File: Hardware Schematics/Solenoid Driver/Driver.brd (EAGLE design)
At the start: 21.6 x 21.6 mm, 6 parts

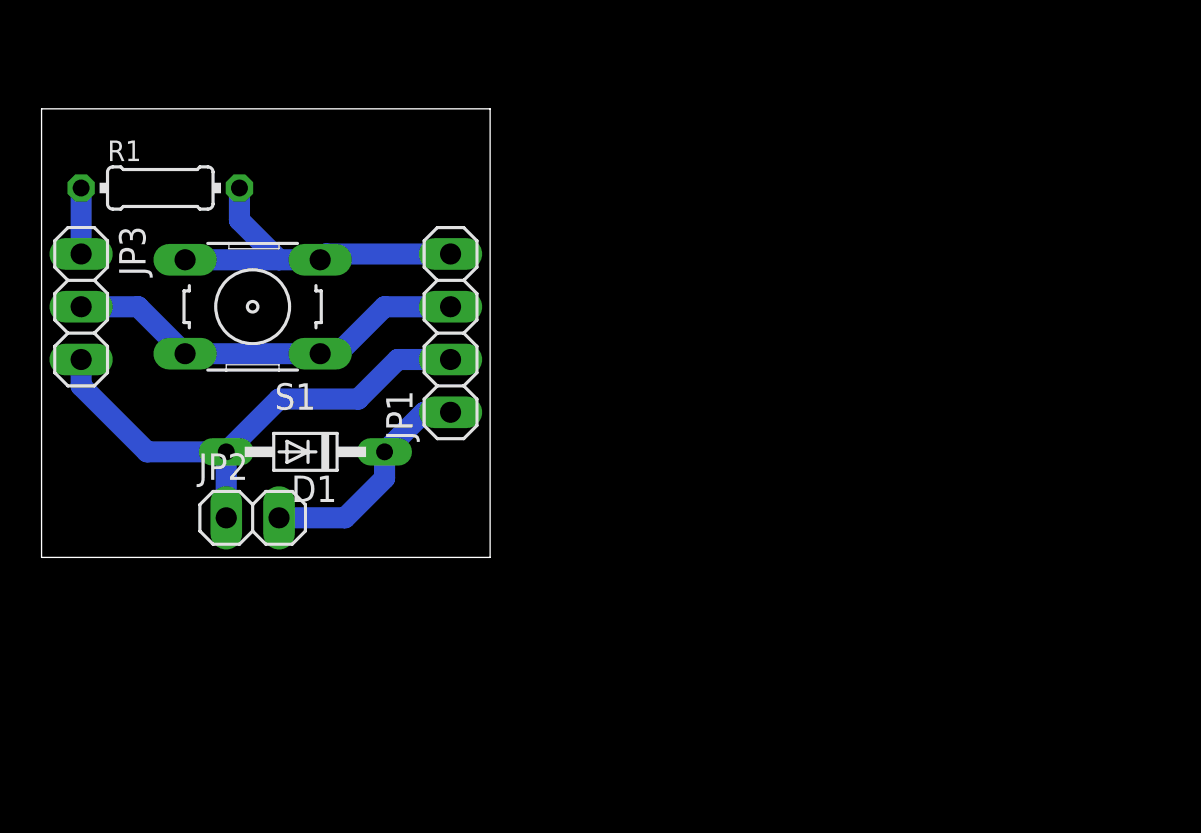
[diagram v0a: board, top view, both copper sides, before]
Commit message: New Solenoid Driver Design
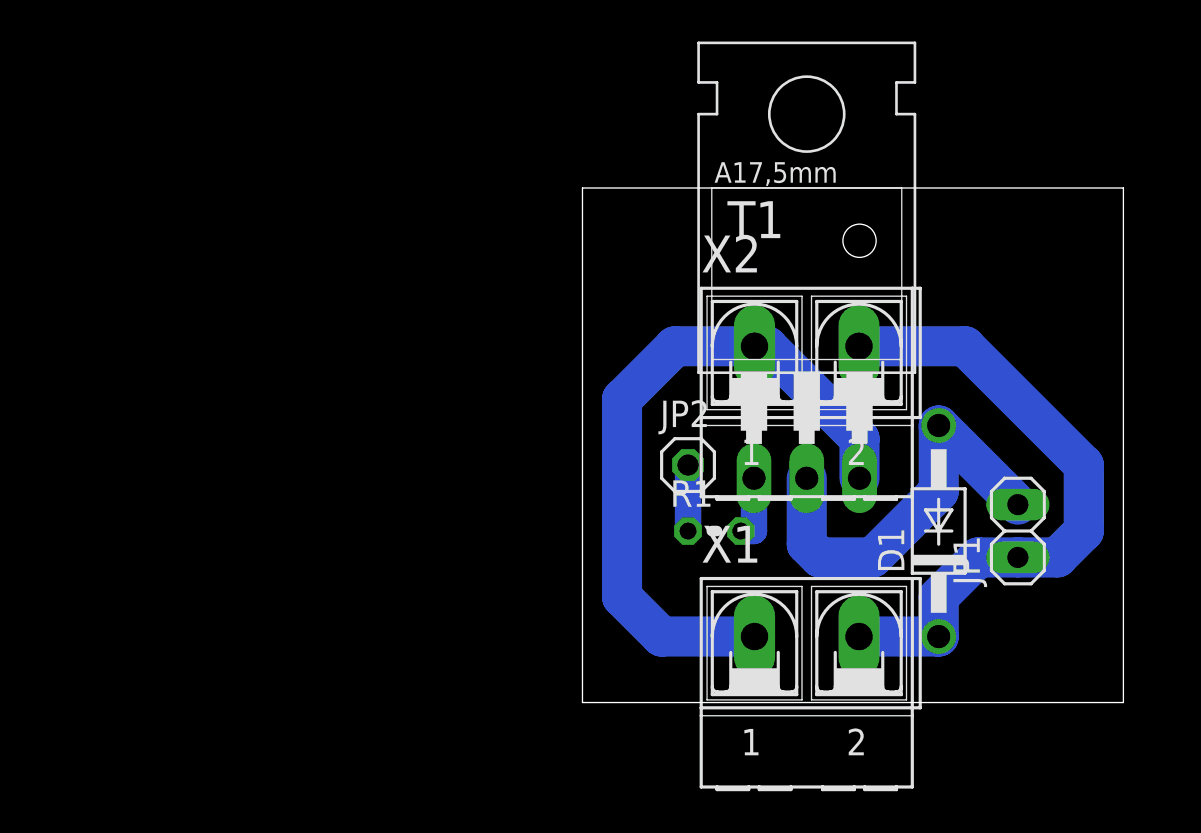
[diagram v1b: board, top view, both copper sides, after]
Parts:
- removed JP3: (no value), pinhead:1X03
- removed S1: (no value), switch-omron:B3F-10XX
- added T1: TIP31, transistor:TO220
- added X1, X2: (no value), con-ptr500:AK500/2-H
- D1: value BAT81 -> 1N4004; device diode:DO34-7 -> diode:DO41-10
- JP1: device pinhead:1X04 -> pinhead:1X02
- JP2: device pinhead:1X02 -> pinhead:1X01
- R1: device resistor:0204/7 -> rcl:0204V
- moved R1 31.4 mm to (46.4, 38.1)
- moved D1 30.7 mm to (57.1, 38.1), turned to 90 degrees
- moved JP1 28.9 mm to (61.0, 38.1)
- moved JP2 21.1 mm to (45.1, 41.3)
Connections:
- removed net ANALOG: JP1.4, R1.2, S1.3, S1.4
- removed net GND: JP1.3, JP3.2, S1.1, S1.2
- removed net L+: D1.C, JP1.1, JP2.2
- removed net L-: D1.A, JP1.2, JP2.1, JP3.3
- new net N$1: D1.A, JP1.2, T1.2
- new net N$3: T1.3, X1.1, X2.1
- new net N$4: JP2.1, R1.1
- new net N$5: D1.C, JP1.1, X1.2, X2.2
- net N$2: now also R1.2, T1.1; no longer JP3.1, R1.1
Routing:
- net N$3: track 0.00 -> 32.9 mm
- net N$5: track 0.00 -> 30.4 mm
- net L-: track 25.4 -> 0.00 mm
- net N$1: track 0.00 -> 19.7 mm
- net GND: track 19.7 -> 0.00 mm
- net ANALOG: track 17.1 -> 0.00 mm
- net L+: track 11.1 -> 0.00 mm
- net N$4: track 0.00 -> 3.17 mm
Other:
- board size 21.6 x 21.6 mm -> 26 x 24.8 mm

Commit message: Updating Repository
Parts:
- removed JP1: (no value), pinhead:1X02
- added X3: (no value), con-ptr500:AK500/2-H
- moved JP2 6.38 mm to (44.5, 34.9)
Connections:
- net N$3 renamed GND
- net N$1: now also X3.2; no longer JP1.2
- net N$5: now also X3.1; no longer JP1.1
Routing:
- net GND: track 32.9 -> 0.00 mm
- net N$1: track 19.7 -> 17.5 mm
- net N$5: track 30.4 -> 29.7 mm
- added copper zone on layer 16, net GND
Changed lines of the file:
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@@
 <layer number="16" name="Bottom" color="1" fill="1" visible="yes" active="yes"/>
 <layer number="17" name="Pads" color="2" fill="1" visible="yes" active="yes"/>
-<layer number="18" name="Vias" color="2" fill="1" visible="no" active="yes"/>
+<layer number="18" name="Vias" color="2" fill="1" visible="yes" active="yes"/>
 <layer number="19" name="Unrouted" color="6" fill="1" visible="no" active="yes"/>
 <layer number="20" name="Dimension" color="15" fill="1" visible="yes" active="yes"/>
@@
 </class>
 </classes>
-<designrules name="default">
+<designrules name="default *">
 <description language="de">&lt;b&gt;EAGLE Design Rules&lt;/b&gt;
 &lt;p&gt;
@@
 <param name="mtCopper" value="0.035mm 0.035mm 0.035mm 0.035mm 0.035mm 0.035mm 0.035mm 0.035mm 0.035mm 0.035mm 0.035mm 0.035mm 0.035mm 0.035mm 0.035mm 0.035mm"/>
 <param name="mtIsolate" value="1.5mm 0.15mm 0.2mm 0.15mm 0.2mm 0.15mm 0.2mm 0.15mm 0.2mm 0.15mm 0.2mm 0.15mm 0.2mm 0.15mm 0.2mm"/>
-<param name="mdWireWire" value="8mil"/>
-<param name="mdWirePad" value="8mil"/>
+<param name="mdWireWire" value="24mil"/>
+<param name="mdWirePad" value="24mil"/>
 <param name="mdWireVia" value="8mil"/>
 <param name="mdPadPad" value="8mil"/>
@@
 <param name="mdViaViaSameLayer" value="8mil"/>
 <param name="mnLayersViaInSmd" value="2"/>
-<param name="mdCopperDimension" value="40mil"/>
-<param name="mdDrill" value="8mil"/>
+<param name="mdCopperDimension" value="24mil"/>
+<param name="mdDrill" value="24mil"/>
 <param name="mdSmdStop" value="0mil"/>
-<param name="msWidth" value="10mil"/>
+<param name="msWidth" value="24mil"/>
 <param name="msDrill" value="24mil"/>
 <param name="msMicroVia" value="9.99mm"/>
@@
 <param name="srMinRoundness" value="0mil"/>
 <param name="srMaxRoundness" value="0mil"/>
-<param name="slThermalIsolate" value="10mil"/>
+<param name="slThermalIsolate" value="0mil"/>
 <param name="slThermalsForVias" value="0"/>
 <param name="dpMaxLengthDifference" value="10mm"/>
@@
 <elements>
 <element name="D1" library="diode" package="DO41-10" value="1N4004" x="57.15" y="38.1" rot="R90"/>
-<element name="JP1" library="pinhead" package="1X02" value="" x="60.96" y="38.1" rot="R90"/>
-<element name="JP2" library="pinhead" package="1X01" value="" x="45.085" y="41.275"/>
+<element name="JP2" library="pinhead" package="1X01" value="" x="44.45" y="34.925"/>
 <element name="R1" library="rcl" package="0204V" value="" x="46.355" y="38.1"/>
 <element name="T1" library="transistor" package="TO220" value="TIP31" x="50.8" y="46.99"/>
@@
 <attribute name="MPN" value="" x="50.8" y="46.99" size="1.778" layer="27" display="off"/>
 </element>
+<element name="X3" library="con-ptr500" package="AK500/2-H" value="" x="60.325" y="37.465" rot="R90">
+<attribute name="OC_NEWARK" value="unknown" x="60.325" y="37.465" size="1.778" layer="27" rot="R90" display="off"/>
+<attribute name="MPN" value="" x="60.325" y="37.465" size="1.778" layer="27" rot="R90" display="off"/>
+<attribute name="OC_FARNELL" value="unknown" x="60.325" y="37.465" size="1.778" layer="27" rot="R90" display="off"/>
+<attribute name="MF" value="" x="60.325" y="37.465" size="1.778" layer="27" rot="R90" display="off"/>
+</element>
 </elements>
 <signals>
@@
 <contactref element="D1" pad="A"/>
 <contactref element="T1" pad="2"/>
-<contactref element="JP1" pad="2"/>
-<wire x1="60.96" y1="39.37" x2="57.15" y2="43.18" width="1.9304" layer="16"/>
 <wire x1="57.15" y1="43.18" x2="57.15" y2="40.005" width="1.9304" layer="16"/>
 <wire x1="57.15" y1="40.005" x2="53.975" y2="36.83" width="1.9304" layer="16"/>
@@
 <wire x1="51.435" y1="36.83" x2="50.8" y2="37.465" width="1.9304" layer="16"/>
 <wire x1="50.8" y1="37.465" x2="50.8" y2="40.64" width="1.9304" layer="16"/>
+<contactref element="X3" pad="2"/>
+<wire x1="60.325" y1="39.9796" x2="57.15" y2="39.9796" width="1.9304" layer="16"/>
+<wire x1="57.15" y1="39.9796" x2="57.15" y2="40.005" width="1.9304" layer="16"/>
 </signal>
 <signal name="N$2">
@@
 <signal name="N$5">
 <contactref element="D1" pad="C"/>
-<contactref element="JP1" pad="1"/>
 <contactref element="X1" pad="2"/>
 <contactref element="X2" pad="2"/>
-<wire x1="57.15" y1="33.02" x2="57.15" y2="34.925" width="1.9304" layer="16"/>
-<wire x1="57.15" y1="34.925" x2="59.055" y2="36.83" width="1.9304" layer="16"/>
-<wire x1="59.055" y1="36.83" x2="60.96" y2="36.83" width="1.9304" layer="16"/>
 <wire x1="53.3146" y1="33.02" x2="57.15" y2="33.02" width="1.9304" layer="16"/>
-<wire x1="60.96" y1="36.83" x2="62.865" y2="36.83" width="1.9304" layer="16"/>
-<wire x1="62.865" y1="36.83" x2="64.135" y2="38.1" width="1.9304" layer="16"/>
-<wire x1="64.135" y1="38.1" x2="64.135" y2="41.275" width="1.9304" layer="16"/>
+<wire x1="64.135" y1="37.465" x2="64.135" y2="41.275" width="1.9304" layer="16"/>
 <wire x1="64.135" y1="41.275" x2="58.42" y2="46.99" width="1.9304" layer="16"/>
 <wire x1="58.42" y1="46.99" x2="53.3146" y2="46.99" width="1.9304" layer="16"/>
+<contactref element="X3" pad="1"/>
+<wire x1="64.135" y1="37.465" x2="61.595" y2="34.925" width="1.9304" layer="16"/>
+<wire x1="61.595" y1="34.925" x2="60.3504" y2="34.925" width="1.9304" layer="16"/>
+<wire x1="60.3504" y1="34.925" x2="60.325" y2="34.9504" width="1.9304" layer="16"/>
+<wire x1="57.15" y1="33.02" x2="58.3946" y2="33.02" width="1.9304" layer="16"/>
+<wire x1="58.3946" y1="33.02" x2="60.325" y2="34.9504" width="1.9304" layer="16"/>
 </signal>
 <signal name="N$4">
 <contactref element="R1" pad="1"/>
 <contactref element="JP2" pad="1"/>
-<wire x1="45.085" y1="38.1" x2="45.085" y2="41.275" width="1.27" layer="16"/>
-</signal>
-<signal name="N$3">
+<wire x1="45.085" y1="38.1" x2="44.45" y2="37.465" width="1.27" layer="16"/>
+<wire x1="44.45" y1="37.465" x2="44.45" y2="34.925" width="1.27" layer="16"/>
+</signal>
+<signal name="GND">
+<polygon width="0.4064" layer="16" orphans="yes">
+<vertex x="40.005" y="54.61"/>
+<vertex x="66.04" y="54.61"/>
+<vertex x="66.04" y="29.845"/>
+<vertex x="40.005" y="29.845"/>
+</polygon>
 <contactref element="T1" pad="3"/>
 <contactref element="X1" pad="1"/>
 <contactref element="X2" pad="1"/>
-<wire x1="53.34" y1="40.64" x2="53.34" y2="42.545" width="1.9304" layer="16"/>
-<wire x1="53.34" y1="42.545" x2="48.895" y2="46.99" width="1.9304" layer="16"/>
-<wire x1="48.895" y1="46.99" x2="48.2854" y2="46.99" width="1.9304" layer="16"/>
-<wire x1="44.45" y1="46.99" x2="48.2854" y2="46.99" width="1.9304" layer="16"/>
-<wire x1="44.45" y1="46.99" x2="41.91" y2="44.45" width="1.9304" layer="16"/>
-<wire x1="41.91" y1="44.45" x2="41.91" y2="34.925" width="1.9304" layer="16"/>
-<wire x1="41.91" y1="34.925" x2="43.815" y2="33.02" width="1.9304" layer="16"/>
-<wire x1="43.815" y1="33.02" x2="48.2854" y2="33.02" width="1.9304" layer="16"/>
 </signal>
 </signals>
-<errors>
-</errors>
 </board>
 </drawing>
